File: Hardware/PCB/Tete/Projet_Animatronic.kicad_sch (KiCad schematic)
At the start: 25 parts, among them J1 Conn_01x06, J101 Conn_01x04, J2 Conn_01x06, J3 Conn_01x06, J4 Conn_01x15, U8 PCA9685PW

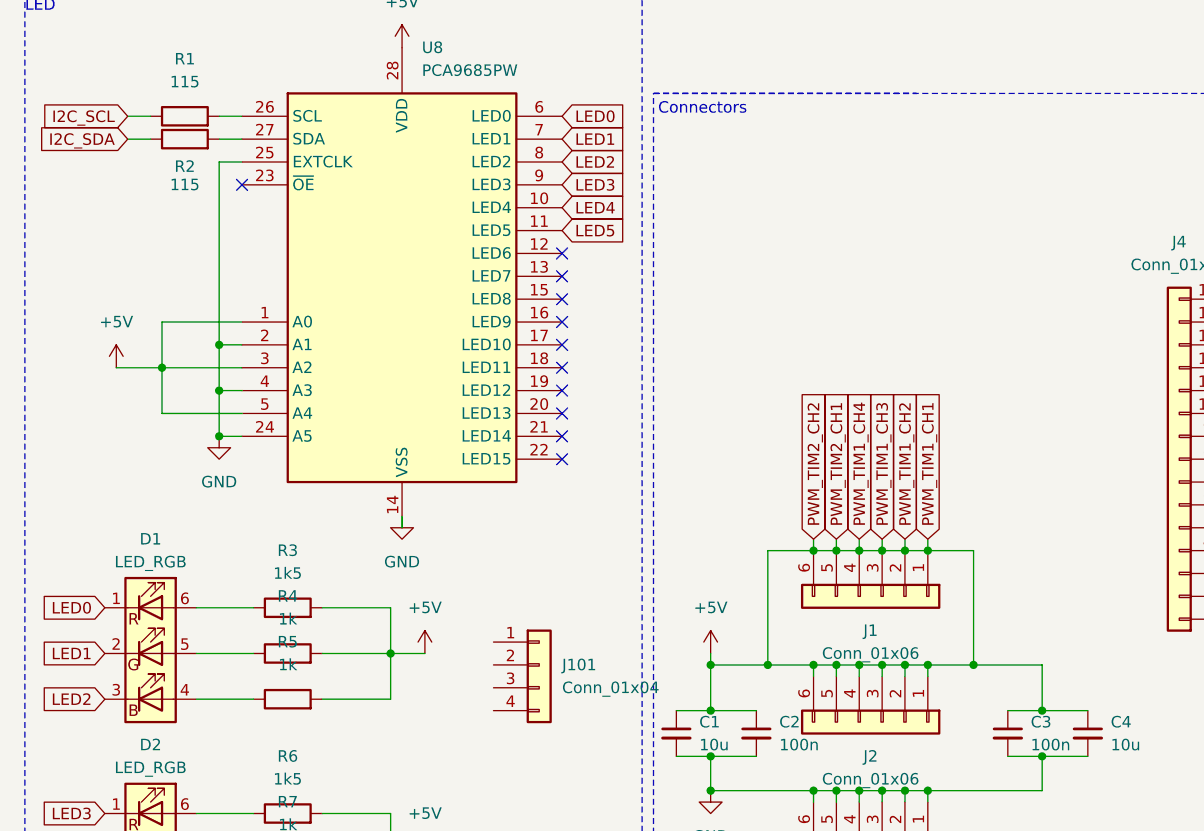
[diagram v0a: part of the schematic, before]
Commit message: change i2c addr led driver conf
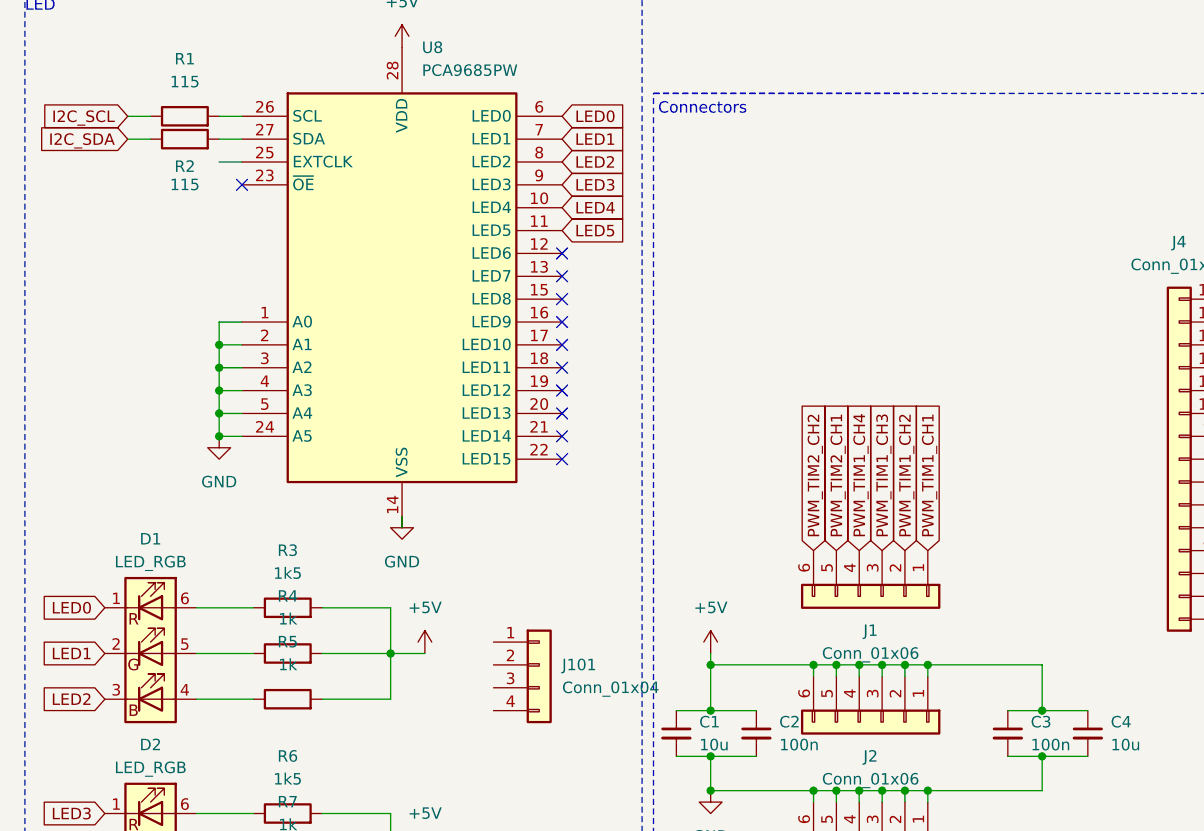
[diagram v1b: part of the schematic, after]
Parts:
- J1, J2, J3: footprint Connector_PinSocket_2.00mm:PinSocket_1x06_P2.00mm_Horizontal -> Connector_PinHeader_2.54mm:PinHeader_1x06_P2.54mm_Vertical
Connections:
- net +5V: no longer J1.1 (Pin_1), J1.2 (Pin_2), J1.3 (Pin_3), J1.4 (Pin_4), J1.5 (Pin_5), J1.6 (Pin_6), J4.2 (Pin_2), J4.3 (Pin_3), J4.4 (Pin_4), J4.5 (Pin_5), J4.6 (Pin_6), J4.7 (Pin_7), U8.1 (A0), U8.3 (A2), U8.5 (A4)
- net GND: now also U8.1 (A0), U8.3 (A2), U8.5 (A4); no longer U8.25 (EXTCLK)
- new net PWM_TIM1_CH1: J1.1 (Pin_1), J4.2 (Pin_2)
- new net PWM_TIM1_CH2: J1.2 (Pin_2), J4.3 (Pin_3)
- new net PWM_TIM1_CH3: J1.3 (Pin_3), J4.4 (Pin_4)
- new net PWM_TIM1_CH4: J1.4 (Pin_4), J4.5 (Pin_5)
- new net PWM_TIM2_CH1: J1.5 (Pin_5), J4.6 (Pin_6)
- new net PWM_TIM2_CH2: J1.6 (Pin_6), J4.7 (Pin_7)
